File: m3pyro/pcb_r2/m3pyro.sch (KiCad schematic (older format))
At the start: 68 parts, among them IC1 STM32F405RxTx, IC2 TPS62130, IC3 MCP2562, IC4 TPS62150, J1 WEST TOP, J2 WEST BOT, J3 EAST TOP, J4 EAST BOT, Q1 Si5515CDC, Q2 Si5515CDC, Q3 Si5515CDC, Q4 Si5515CDC, Q5 Si5515CDC, Q6 Si5515CDC, Q7 Si5515CDC, Q8 Si5515CDC, Y1 26M

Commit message: m3pyro r2 routing progress
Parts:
- removed R1, R6: 10k, agg:0402, symbol R
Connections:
- net 1A_EN: now also IC1.43 (PA10)
- net 3A_EN: now also IC1.45 (PA12)
- net 3v3: now also IC1.59 (PB7)
- net BUS_DIV: now also IC1.21 (PA5), IC1.42 (PA9)
- net CH1: now also IC1.34 (PB13)
- net CH2: now also IC1.36 (PB15)
- net CH3: now also IC1.30 (PB11)
- net CH4: now also IC1.38 (PC7)
- net CH5: now also IC1.35 (PB14)
- net CH6: now also IC1.37 (PC6)
- net CH7: now also IC1.33 (PB12)
- net CH8: now also IC1.39 (PC8)
- net CONT: now also IC1.22 (PA6), IC1.41 (PA8)
- net CONT_EN: now also IC1.23 (PA7), IC1.40 (PC9)
- net GND: now also IC2.5 (FB), IC4.5 (FB)
- net SI_DIV: now also IC1.20 (PA4), IC1.44 (PA11)
- no-connect marks 8 -> 6
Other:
- note added: "PASSTHROUGH"

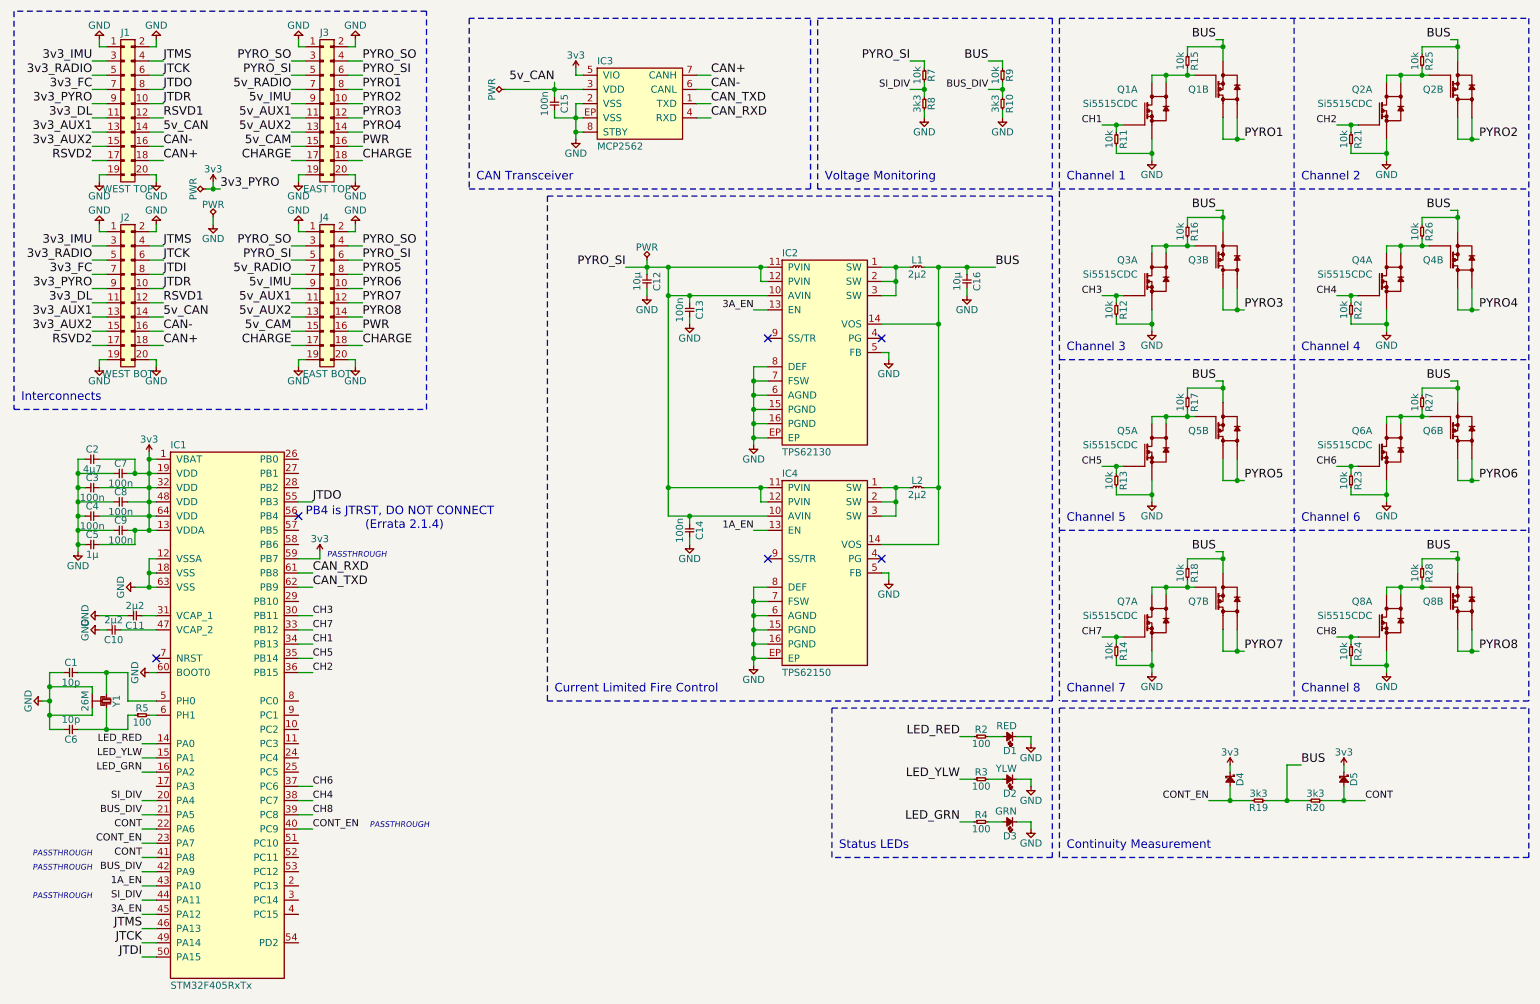
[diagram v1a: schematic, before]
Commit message: fully routed m3pyro
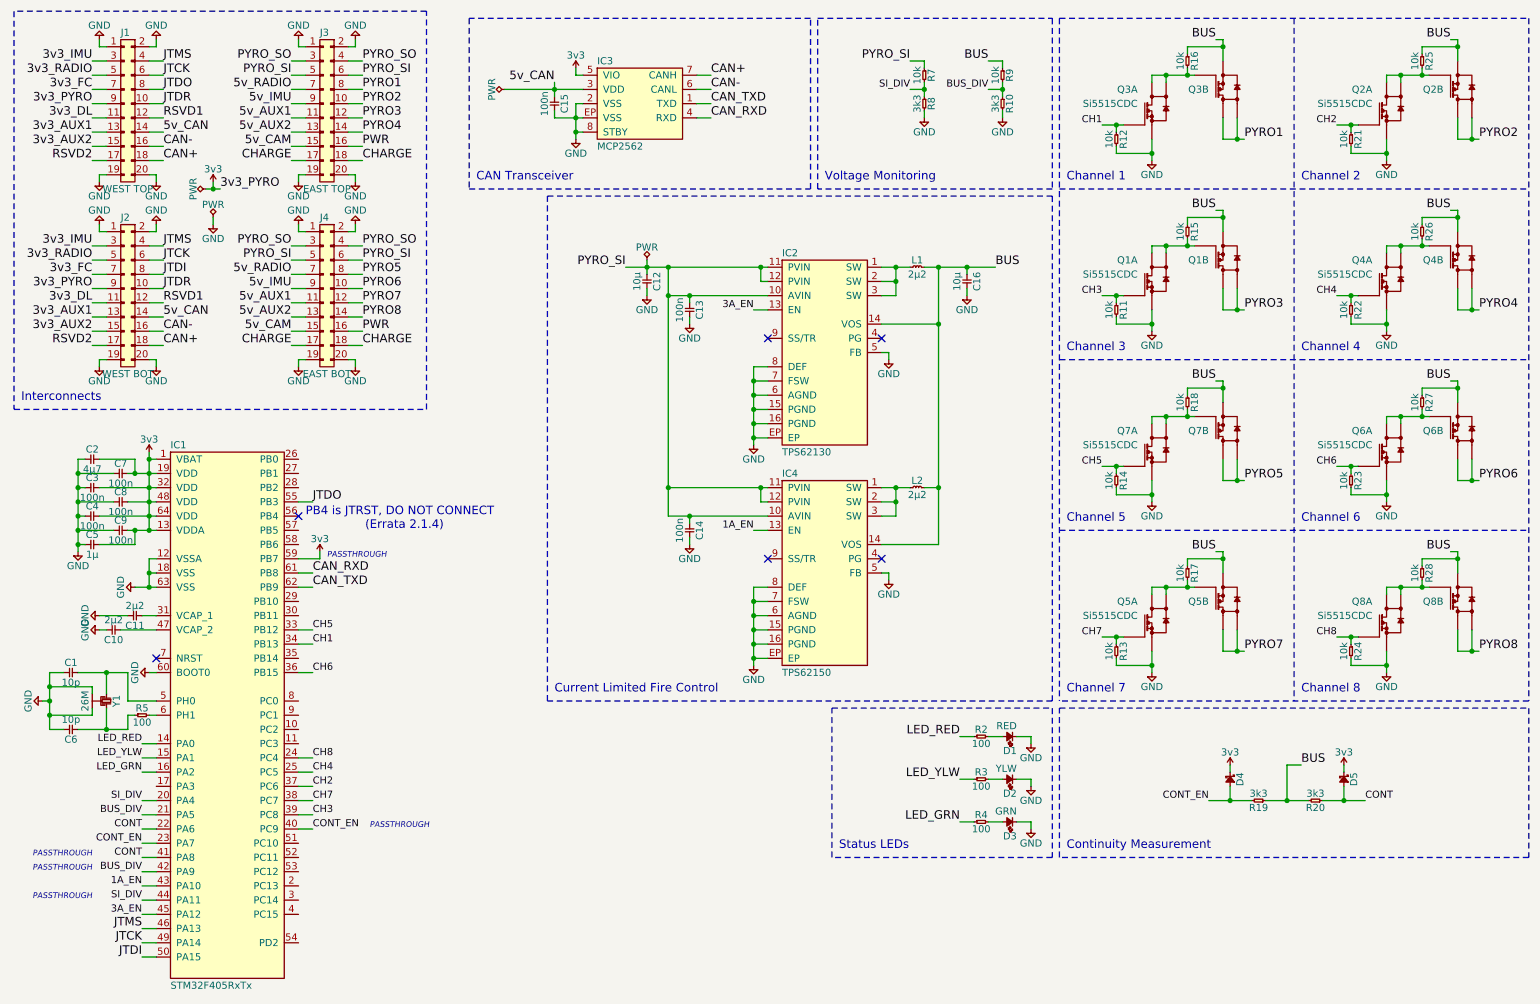
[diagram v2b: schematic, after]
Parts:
- renumbered Q3 to Q1, Q1 to Q3, Q7 to Q5, Q5 to Q7, R12 to R11, R11 to R12, R14 to R13, R13 to R14, R16 to R15, R15 to R16, R18 to R17, R17 to R18
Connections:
- net CH2: now also IC1.37 (PC6); no longer IC1.36 (PB15)
- net CH3: now also IC1.39 (PC8); no longer IC1.30 (PB11)
- net CH4: now also IC1.25 (PC5); no longer IC1.38 (PC7)
- net CH5: now also IC1.33 (PB12); no longer IC1.35 (PB14)
- net CH6: now also IC1.36 (PB15); no longer IC1.37 (PC6)
- net CH7: now also IC1.38 (PC7); no longer IC1.33 (PB12)
- net CH8: now also IC1.24 (PC4); no longer IC1.39 (PC8)
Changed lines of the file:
@@
 CONT
 $Comp
-L Si5515CDC Q1
+L Si5515CDC Q3
 U 2 1 596782EF
 P 9000 1050
-F 0 "Q1" H 8900 1050 50  0000 R CNN
+F 0 "Q3" H 8900 1050 50  0000 R CNN
 F 1 "Si5515CDC" V 9200 1050 50  0001 C CNN
 F 2 "agg:ChipFET-1206-8" H 9000 300 50  0001 C CNN
@@
 $EndComp
 $Comp
-L Si5515CDC Q1
+L Si5515CDC Q3
 U 1 1 596789B6
 P 8500 1200
-F 0 "Q1" H 8400 1350 50  0000 R CNN
+F 0 "Q3" H 8400 1350 50  0000 R CNN
 F 1 "Si5515CDC" H 8400 1250 50  0000 R CNN
 F 2 "agg:ChipFET-1206-8" H 8500 450 50  0001 C CNN
@@
 $EndComp
 $Comp
-L R R11
+L R R12
 U 1 1 59679194
 P 8250 1350
-F 0 "R11" H 8300 1400 50  0000 C CNN
+F 0 "R12" H 8300 1400 50  0000 C CNN
 F 1 "10k" H 8300 1300 50  0000 C CNN
 F 2 "agg:0402" H 8250 1350 50  0001 C CNN
@@
 Connection ~ 8600 950
 $Comp
-L R R15
+L R R16
 U 1 1 5967A991
 P 8750 800
-F 0 "R15" H 8800 850 50  0000 C CNN
+F 0 "R16" H 8800 850 50  0000 C CNN
 F 1 "10k" H 8800 750 50  0000 C CNN
 F 2 "agg:0402" H 8750 800 50  0001 C CNN
@@
 Channel 2
 $Comp
-L Si5515CDC Q3
+L Si5515CDC Q1
 U 2 1 5967F3CD
 P 9000 2250
-F 0 "Q3" H 8900 2250 50  0000 R CNN
+F 0 "Q1" H 8900 2250 50  0000 R CNN
 F 1 "Si5515CDC" V 9200 2250 50  0001 C CNN
 F 2 "agg:ChipFET-1206-8" H 9000 1500 50  0001 C CNN
@@
 $EndComp
 $Comp
-L Si5515CDC Q3
+L Si5515CDC Q1
 U 1 1 5967F3D4
 P 8500 2400
-F 0 "Q3" H 8400 2550 50  0000 R CNN
+F 0 "Q1" H 8400 2550 50  0000 R CNN
 F 1 "Si5515CDC" H 8400 2450 50  0000 R CNN
 F 2 "agg:ChipFET-1206-8" H 8500 1650 50  0001 C CNN
@@
 $EndComp
 $Comp
-L R R12
+L R R11
 U 1 1 5967F3DA
 P 8250 2550
-F 0 "R12" H 8300 2600 50  0000 C CNN
+F 0 "R11" H 8300 2600 50  0000 C CNN
 F 1 "10k" H 8300 2500 50  0000 C CNN
 F 2 "agg:0402" H 8250 2550 50  0001 C CNN
@@
 Connection ~ 8600 2150
 $Comp
-L R R16
+L R R15
 U 1 1 5967F3F1
 P 8750 2000
-F 0 "R16" H 8800 2050 50  0000 C CNN
+F 0 "R15" H 8800 2050 50  0000 C CNN
 F 1 "10k" H 8800 1950 50  0000 C CNN
 F 2 "agg:0402" H 8750 2000 50  0001 C CNN
@@
 Channel 4
 $Comp
-L Si5515CDC Q5
+L Si5515CDC Q7
 U 2 1 596805B7
 P 9000 3450
-F 0 "Q5" H 8900 3450 50  0000 R CNN
+F 0 "Q7" H 8900 3450 50  0000 R CNN
 F 1 "Si5515CDC" V 9200 3450 50  0001 C CNN
 F 2 "agg:ChipFET-1206-8" H 9000 2700 50  0001 C CNN
@@
 $EndComp
 $Comp
-L Si5515CDC Q5
+L Si5515CDC Q7
 U 1 1 596805BE
 P 8500 3600
-F 0 "Q5" H 8400 3750 50  0000 R CNN
+F 0 "Q7" H 8400 3750 50  0000 R CNN
 F 1 "Si5515CDC" H 8400 3650 50  0000 R CNN
 F 2 "agg:ChipFET-1206-8" H 8500 2850 50  0001 C CNN
@@
 $EndComp
 $Comp
-L R R13
+L R R14
 U 1 1 596805C4
 P 8250 3750
-F 0 "R13" H 8300 3800 50  0000 C CNN
+F 0 "R14" H 8300 3800 50  0000 C CNN
 F 1 "10k" H 8300 3700 50  0000 C CNN
 F 2 "agg:0402" H 8250 3750 50  0001 C CNN
@@
 Connection ~ 8600 3350
 $Comp
-L R R17
+L R R18
 U 1 1 596805DB
 P 8750 3200
-F 0 "R17" H 8800 3250 50  0000 C CNN
+F 0 "R18" H 8800 3250 50  0000 C CNN
 F 1 "10k" H 8800 3150 50  0000 C CNN
 F 2 "agg:0402" H 8750 3200 50  0001 C CNN
@@
 Channel 6
 $Comp
-L Si5515CDC Q7
+L Si5515CDC Q5
 U 2 1 59680630
 P 9000 4650
-F 0 "Q7" H 8900 4650 50  0000 R CNN
+F 0 "Q5" H 8900 4650 50  0000 R CNN
 F 1 "Si5515CDC" V 9200 4650 50  0001 C CNN
 F 2 "agg:ChipFET-1206-8" H 9000 3900 50  0001 C CNN
@@
 $EndComp
 $Comp
-L Si5515CDC Q7
+L Si5515CDC Q5
 U 1 1 59680637
 P 8500 4800
-F 0 "Q7" H 8400 4950 50  0000 R CNN
+F 0 "Q5" H 8400 4950 50  0000 R CNN
 F 1 "Si5515CDC" H 8400 4850 50  0000 R CNN
 F 2 "agg:ChipFET-1206-8" H 8500 4050 50  0001 C CNN
@@
 $EndComp
 $Comp
-L R R14
+L R R13
 U 1 1 5968063D
 P 8250 4950
-F 0 "R14" H 8300 5000 50  0000 C CNN
+F 0 "R13" H 8300 5000 50  0000 C CNN
 F 1 "10k" H 8300 4900 50  0000 C CNN
 F 2 "agg:0402" H 8250 4950 50  0001 C CNN
@@
 Connection ~ 8600 4550
 $Comp
-L R R18
+L R R17
 U 1 1 59680654
 P 8750 4400
-F 0 "R18" H 8800 4450 50  0000 C CNN
+F 0 "R17" H 8800 4450 50  0000 C CNN
 F 1 "10k" H 8800 4350 50  0000 C CNN
 F 2 "agg:0402" H 8750 4400 50  0001 C CNN
@@
 Text Label 2600 4950 0    50   ~ 0
 CH1
+Text Label 2600 5950 0    50   ~ 0
+CH2
+Text Label 2600 6150 0    50   ~ 0
+CH3
+Text Label 2600 5850 0    50   ~ 0
+CH4
+Text Label 2600 4850 0    50   ~ 0
+CH5
 Text Label 2600 5150 0    50   ~ 0
-CH2
-Text Label 2600 4750 0    50   ~ 0
-CH3
+CH6
 Text Label 2600 6050 0    50   ~ 0
-CH4
-Text Label 2600 5050 0    50   ~ 0
-CH5
-Text Label 2600 5950 0    50   ~ 0
-CH6
-Text Label 2600 4850 0    50   ~ 0
 CH7
-Text Label 2600 6150 0    50   ~ 0
+Text Label 2600 5750 0    50   ~ 0
 CH8
 Wire Notes Line
@@
 	2500 6250 2600 6250
 Wire Wire Line
-	2600 6150 2500 6150
-Wire Wire Line
-	2500 6050 2600 6050
-Wire Wire Line
-	2600 5950 2500 5950
-Wire Wire Line
-	2500 5150 2600 5150
-Wire Wire Line
-	2600 5050 2500 5050
+	2600 5750 2500 5750
+Wire Wire Line
+	2500 5850 2600 5850
+Wire Wire Line
+	2600 5150 2500 5150
+Wire Wire Line
+	2500 5950 2600 5950
+Wire Wire Line
+	2600 4850 2500 4850
 Wire Wire Line
 	2500 4950 2600 4950
 Wire Wire Line
-	2600 4850 2500 4850
-Wire Wire Line
-	2500 4750 2600 4750
+	2600 6050 2500 6050
+Wire Wire Line
+	2500 6150 2600 6150
 $Comp
 L PWR #FLG052

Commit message: silk, tidyup, etc
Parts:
- added C17: 10µ, agg:0603, symbol C
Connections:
- net GND: now also C17.2
- net PYRO_SI: now also C17.1

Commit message: Amend SMPS output cap on m3pyro r2 to 22u
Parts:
- C16: value 10µ -> 22µ
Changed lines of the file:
@@
 P 7200 2350
 F 0 "C16" H 7250 2420 50  0000 C CNN
-F 1 "10µ" H 7250 2280 50  0000 C CNN
+F 1 "22µ" H 7250 2280 50  0000 C CNN
 F 2 "agg:0603" H 7200 2350 50  0001 C CNN
 F 3 "" H 7200 2350 50  0001 C CNN
